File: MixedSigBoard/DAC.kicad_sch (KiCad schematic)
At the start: 17 parts

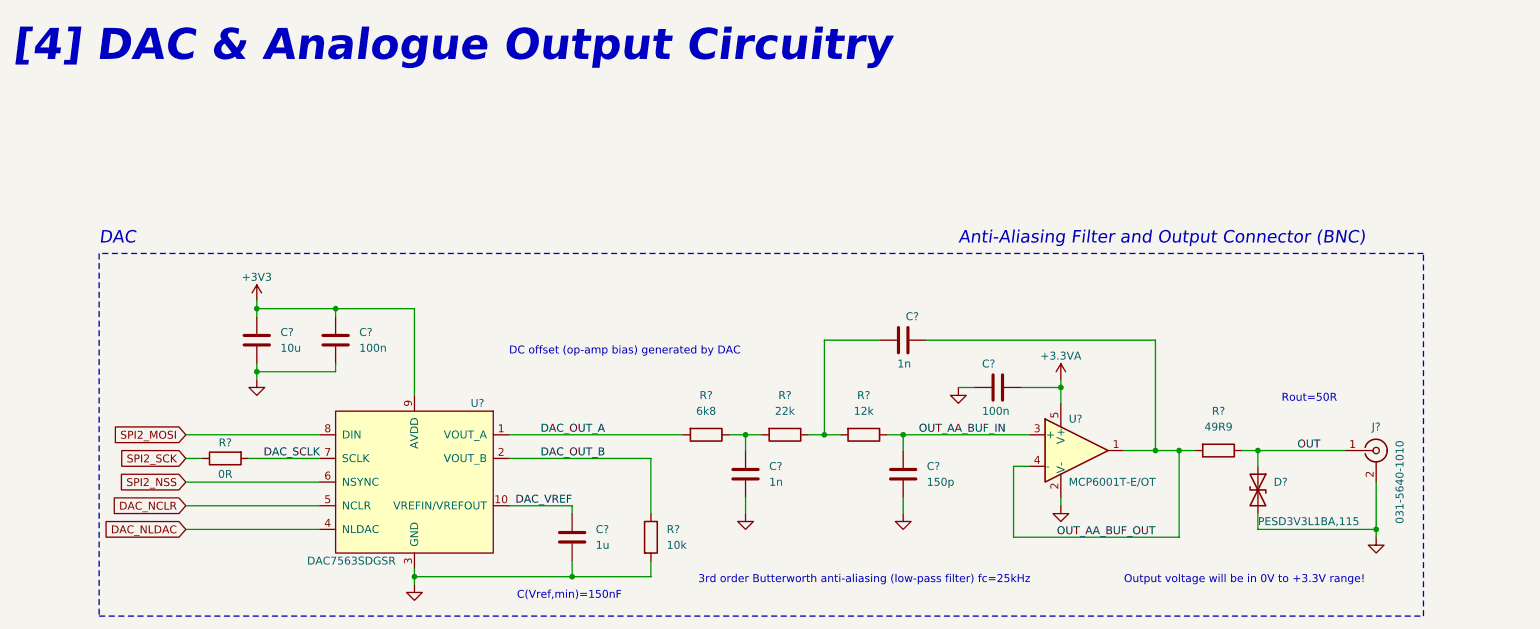
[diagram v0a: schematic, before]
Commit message: -Renumber components to match sheet number -Created PCB Constraints and Set-up
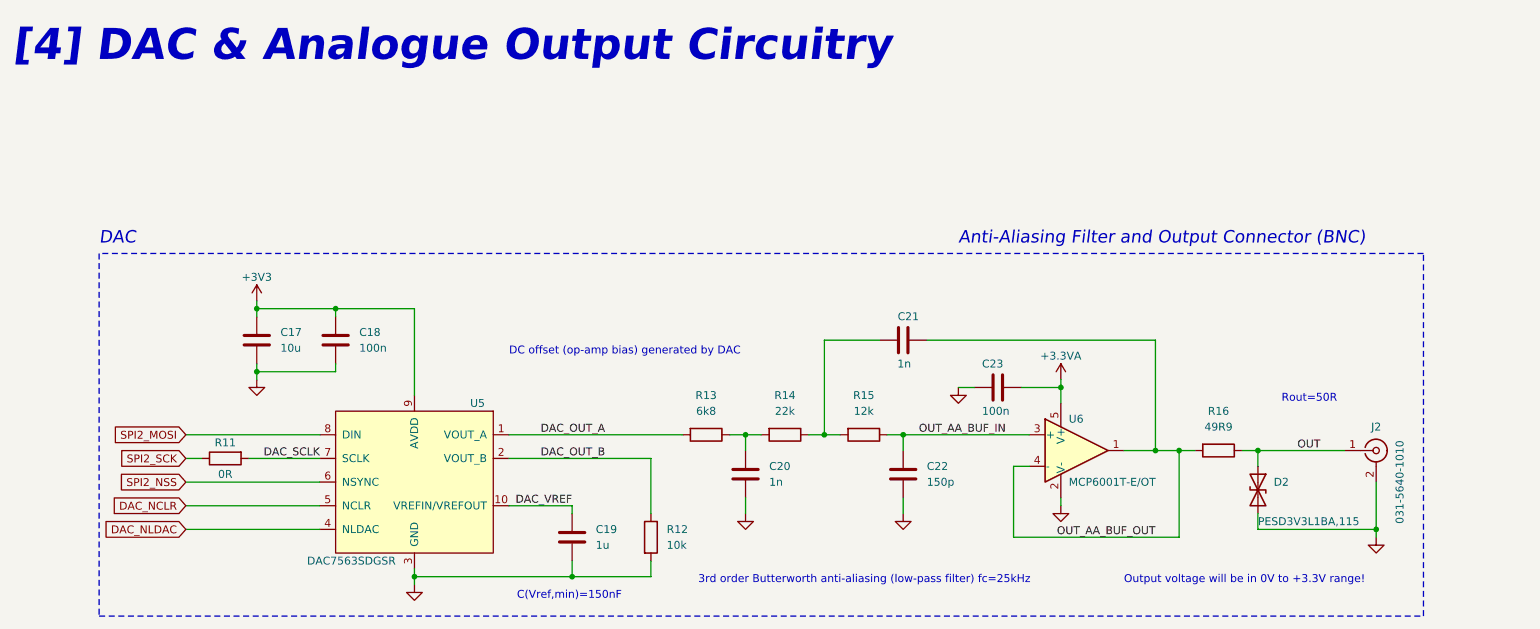
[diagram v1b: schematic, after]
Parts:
- gave numbers to parts that had none: 17

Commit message: Add all footprints
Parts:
- J2: footprint PhilsLab_Footprints_KiCad6:AMPHENOL-BNC-031-5640-1010 -> MixSig_Footprints_KiCad6:AMPHENOL-BNC-031-5640-1010
- U5: footprint PhilsLab_Footprints_KiCad6:VSSOP-10 -> MixSig_Footprints_KiCad6:VSSOP-10
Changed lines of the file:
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@@
 			)
 		)
-		(property "Footprint" "PhilsLab_Footprints_KiCad6:VSSOP-10"
+		(property "Footprint" "MixSig_Footprints_KiCad6:VSSOP-10"
 			(at 88.9 105.41 0)
 			(effects
@@
 			)
 		)
-		(property "Footprint" "PhilsLab_Footprints_KiCad6:AMPHENOL-BNC-031-5640-1010"
+		(property "Footprint" "MixSig_Footprints_KiCad6:AMPHENOL-BNC-031-5640-1010"
 			(at 243.84 95.25 0)
 			(effects

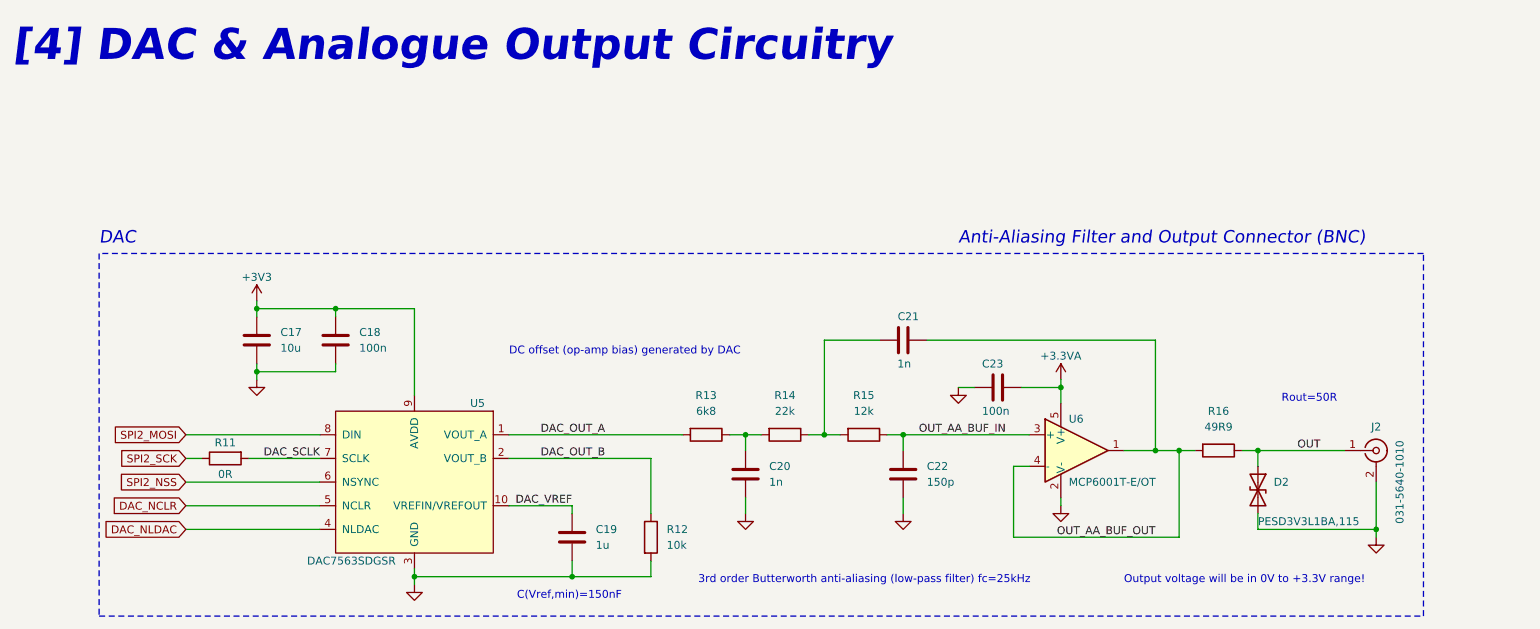
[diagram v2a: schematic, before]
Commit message: Layout w/o Traces for MCU, ADC page
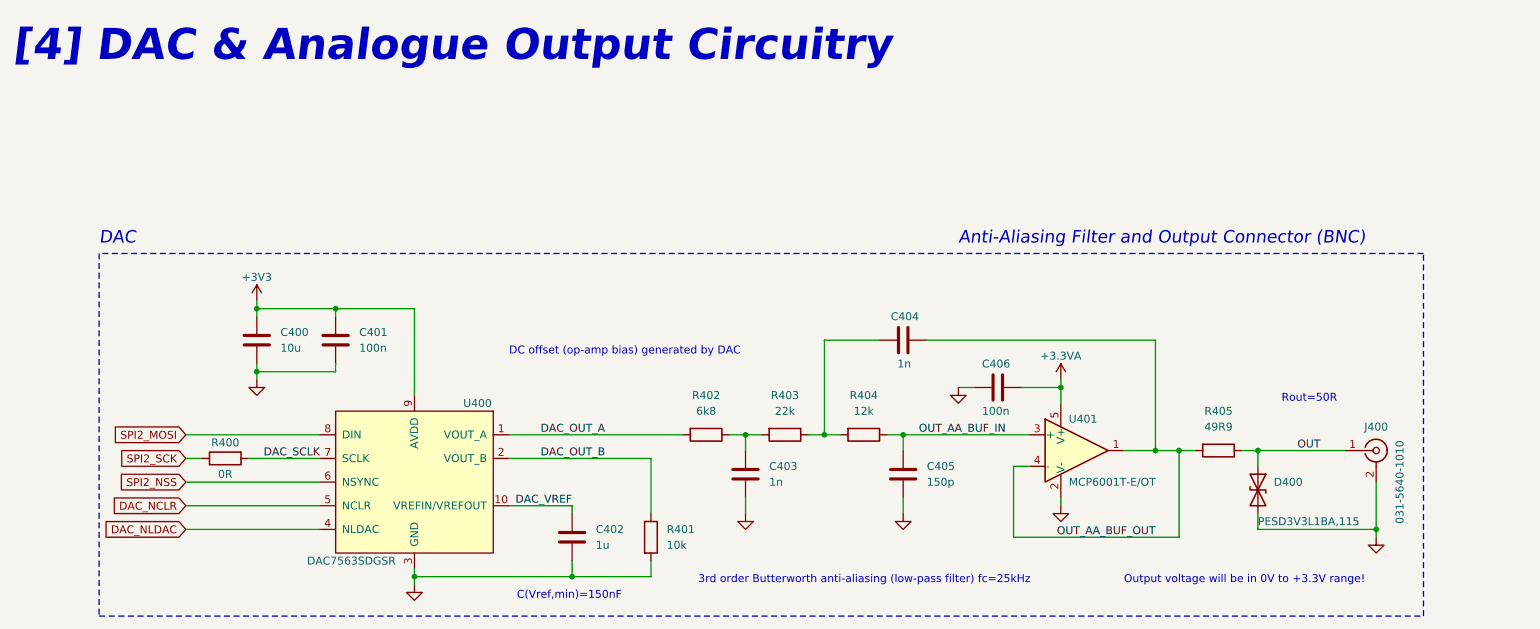
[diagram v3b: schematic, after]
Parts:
- renumbered C17 to C400, C18 to C401, C19 to C402, C20 to C403, C21 to C404, C22 to C405, C23 to C406, D2 to D400, J2 to J400, R11 to R400, R12 to R401, R13 to R402, R14 to R403, R15 to R404, R16 to R405, U5 to U400, U6 to U401
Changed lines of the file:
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@@
 		(on_board yes)
 		(dnp no)
-		(property "Reference" "R11"
+		(property "Reference" "R400"
 			(at 58.42 93.98 90)
 			(effects
@@
 			(project "MixSigPCB"
 				(path "/c49d23ab-146d-4089-864f-2d22b5b414b9/00000000-0000-0000-0000-000061c5ccf5"
-					(reference "R11")
+					(reference "R400")
 					(unit 1)
 				)
@@
 		(on_board yes)
 		(dnp no)
-		(property "Reference" "C19"
+		(property "Reference" "C402"
 			(at 118.11 107.95 0)
 			(effects
@@
 			(project "MixSigPCB"
 				(path "/c49d23ab-146d-4089-864f-2d22b5b414b9/00000000-0000-0000-0000-000061c5ccf5"
-					(reference "C19")
+					(reference "C402")
 					(unit 1)
 				)
@@
 		(on_board yes)
 		(dnp no)
-		(property "Reference" "C17"
+		(property "Reference" "C400"
 			(at 67.31 76.2 0)
 			(effects
@@
 			(project "MixSigPCB"
 				(path "/c49d23ab-146d-4089-864f-2d22b5b414b9/00000000-0000-0000-0000-000061c5ccf5"
-					(reference "C17")
+					(reference "C400")
 					(unit 1)
 				)
@@
 		(on_board yes)
 		(dnp no)
-		(property "Reference" "U5"
+		(property "Reference" "U400"
 			(at 99.06 87.63 0)
 			(effects
@@
 			(project "MixSigPCB"
 				(path "/c49d23ab-146d-4089-864f-2d22b5b414b9/00000000-0000-0000-0000-000061c5ccf5"
-					(reference "U5")
+					(reference "U400")
 					(unit 1)
 				)
@@
 		(on_board yes)
 		(dnp no)
-		(property "Reference" "C18"
+		(property "Reference" "C401"
 			(at 80.01 76.2 0)
 			(effects
@@
 			(project "MixSigPCB"
 				(path "/c49d23ab-146d-4089-864f-2d22b5b414b9/00000000-0000-0000-0000-000061c5ccf5"
-					(reference "C18")
+					(reference "C401")
 					(unit 1)
 				)
@@
 		(on_board yes)
 		(dnp no)
-		(property "Reference" "R12"
+		(property "Reference" "R401"
 			(at 129.54 107.95 0)
 			(effects
@@
 			(project "MixSigPCB"
 				(path "/c49d23ab-146d-4089-864f-2d22b5b414b9/00000000-0000-0000-0000-000061c5ccf5"
-					(reference "R12")
+					(reference "R401")
 					(unit 1)
 				)
@@
 		(on_board yes)
 		(dnp no)
-		(property "Reference" "U6"
+		(property "Reference" "U401"
 			(at 194.31 90.17 0)
 			(effects
@@
 			(project "MixSigPCB"
 				(path "/c49d23ab-146d-4089-864f-2d22b5b414b9/00000000-0000-0000-0000-000061c5ccf5"
-					(reference "U6")
+					(reference "U401")
 					(unit 1)
 				)
@@
 		(on_board yes)
 		(dnp no)
-		(property "Reference" "C23"
+		(property "Reference" "C406"
 			(at 180.34 81.28 90)
 			(effects
@@
 			(project "MixSigPCB"
 				(path "/c49d23ab-146d-4089-864f-2d22b5b414b9/00000000-0000-0000-0000-000061c5ccf5"
-					(reference "C23")
+					(reference "C406")
 					(unit 1)
 				)
@@
 		(on_board yes)
 		(dnp no)
-		(property "Reference" "R13"
+		(property "Reference" "R402"
 			(at 135.89 86.36 90)
 			(effects
@@
 			(project "MixSigPCB"
 				(path "/c49d23ab-146d-4089-864f-2d22b5b414b9/00000000-0000-0000-0000-000061c5ccf5"
-					(reference "R13")
+					(reference "R402")
 					(unit 1)
 				)
@@
 		(on_board yes)
 		(dnp no)
-		(property "Reference" "C20"
+		(property "Reference" "C403"
 			(at 146.05 97.79 0)
 			(effects
@@
 			(project "MixSigPCB"
 				(path "/c49d23ab-146d-4089-864f-2d22b5b414b9/00000000-0000-0000-0000-000061c5ccf5"
-					(reference "C20")
+					(reference "C403")
 					(unit 1)
 				)
@@
 		(on_board yes)
 		(dnp no)
-		(property "Reference" "R14"
+		(property "Reference" "R403"
 			(at 148.59 86.36 90)
 			(effects
@@
 			(project "MixSigPCB"
 				(path "/c49d23ab-146d-4089-864f-2d22b5b414b9/00000000-0000-0000-0000-000061c5ccf5"
-					(reference "R14")
+					(reference "R403")
 					(unit 1)
 				)
@@
 		(on_board yes)
 		(dnp no)
-		(property "Reference" "R15"
+		(property "Reference" "R404"
 			(at 161.29 86.36 90)
 			(effects
@@
 			(project "MixSigPCB"
 				(path "/c49d23ab-146d-4089-864f-2d22b5b414b9/00000000-0000-0000-0000-000061c5ccf5"
-					(reference "R15")
+					(reference "R404")
 					(unit 1)
 				)
@@
 		(on_board yes)
 		(dnp no)
-		(property "Reference" "C22"
+		(property "Reference" "C405"
 			(at 171.45 97.79 0)
 			(effects
@@
 			(project "MixSigPCB"
 				(path "/c49d23ab-146d-4089-864f-2d22b5b414b9/00000000-0000-0000-0000-000061c5ccf5"
-					(reference "C22")
+					(reference "C405")
 					(unit 1)
 				)
@@
 		(on_board yes)
 		(dnp no)
-		(property "Reference" "R16"
+		(property "Reference" "R405"
 			(at 218.44 88.9 90)
 			(effects
@@
 			(project "MixSigPCB"
 				(path "/c49d23ab-146d-4089-864f-2d22b5b414b9/00000000-0000-0000-0000-000061c5ccf5"
-					(reference "R16")
+					(reference "R405")
 					(unit 1)
 				)
@@
 		(on_board yes)
 		(dnp no)
-		(property "Reference" "D2"
+		(property "Reference" "D400"
 			(at 227.33 100.33 90)
 			(effects
@@
 			(project "MixSigPCB"
 				(path "/c49d23ab-146d-4089-864f-2d22b5b414b9/00000000-0000-0000-0000-000061c5ccf5"
-					(reference "D2")
+					(reference "D400")
 					(unit 1)
 				)
@@
 		(on_board yes)
 		(dnp no)
-		(property "Reference" "J2"
+		(property "Reference" "J400"
 			(at 243.84 91.44 0)
 			(effects
@@
 			(project "MixSigPCB"
 				(path "/c49d23ab-146d-4089-864f-2d22b5b414b9/00000000-0000-0000-0000-000061c5ccf5"
-					(reference "J2")
+					(reference "J400")
 					(unit 1)
 				)
@@
 		(on_board yes)
 		(dnp no)
-		(property "Reference" "C21"
+		(property "Reference" "C404"
 			(at 170.18 73.66 90)
 			(effects
@@
 			(project "MixSigPCB"
 				(path "/c49d23ab-146d-4089-864f-2d22b5b414b9/00000000-0000-0000-0000-000061c5ccf5"
-					(reference "C21")
-					(unit 1)
-				)
+					(reference "C404")
+					(unit 1)
+				)

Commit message: updated PCB footprints
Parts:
- J400: footprint MixSig_Footprints_KiCad6:AMPHENOL-BNC-031-5640-1010 -> MixSig_Footprints.pretty:AMPHENOL-BNC-031-5640-1010
- U400: footprint MixSig_Footprints_KiCad6:VSSOP-10 -> MixSig_Footprints.pretty:VSSOP-10
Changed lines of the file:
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@@
 			)
 		)
-		(property "Footprint" "MixSig_Footprints_KiCad6:VSSOP-10"
+		(property "Footprint" "MixSig_Footprints.pretty:VSSOP-10"
 			(at 88.9 105.41 0)
 			(effects
@@
 			)
 		)
-		(property "Footprint" "MixSig_Footprints_KiCad6:AMPHENOL-BNC-031-5640-1010"
+		(property "Footprint" "MixSig_Footprints.pretty:AMPHENOL-BNC-031-5640-1010"
 			(at 243.84 95.25 0)
 			(effects

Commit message: complete the MixSigPCB
-Created Gerber file and compressed to .zip
-created placement file
-filled all components from Mouser/JLCPCB/Digikey
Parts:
- C400: Manufacturer (none) -> TAIYO YUDEN; Manufacturer Part Number (none) -> MLASL168BB5106MTNB33
- C401, C406: Manufacturer (none) -> TAIYO YUDEN; Manufacturer Part Number (none) -> LMK105B7104KVHF
- C402: Manufacturer (none) -> YAGEO; Manufacturer Part Number (none) -> CC0603KRX5R6BB105
- C403, C404: Manufacturer (none) -> KYOCERA AVX; Manufacturer Part Number (none) -> 04025C102KAZ2A
- C405: Manufacturer (none) -> KEMET; Manufacturer Part Number (none) -> C0402C151J1GACAUTO
- D400: Manufacturer (none) -> NEXPERIA USA INC.; Manufacturer Part Number (none) -> PESD3V3L1BA,115
- J400: Manufacturer (none) -> AMPHENOL RF; Manufacturer Part Number (none) -> 31-5640-1010
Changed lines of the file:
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@@
 			)
 		)
-		(property "Datasheet" "~"
+		(property "Datasheet" "https://www.mouser.com/datasheet/3/508/1/upy-gphc_x5r_4v-to-50v.pdf"
 			(at 114.3 109.22 0)
 			(effects
@@
 					(size 1.27 1.27)
 				)
+			)
+		)
+		(property "Manufacturer" "YAGEO"
+			(at 114.3 109.22 0)
+			(effects
+				(font
+					(size 1.27 1.27)
+				)
+				(hide yes)
+			)
+		)
+		(property "Manufacturer Part Number" "CC0603KRX5R6BB105"
+			(at 114.3 109.22 0)
+			(effects
+				(font
+					(size 1.27 1.27)
+				)
+				(hide yes)
 			)
 		)
@@
 			)
 		)
-		(property "Datasheet" "~"
+		(property "Datasheet" "https://ds.yuden.co.jp/TYCOMPAS/or/download?pn=MLAST063SCG681JFNA01&fileType=CA"
 			(at 63.5 77.47 0)
 			(effects
@@
 					(size 1.27 1.27)
 				)
+			)
+		)
+		(property "Manufacturer" "TAIYO YUDEN"
+			(at 63.5 77.47 0)
+			(effects
+				(font
+					(size 1.27 1.27)
+				)
+				(hide yes)
+			)
+		)
+		(property "Manufacturer Part Number" "MLASL168BB5106MTNB33"
+			(at 63.5 77.47 0)
+			(effects
+				(font
+					(size 1.27 1.27)
+				)
+				(hide yes)
 			)
 		)
@@
 			)
 		)
-		(property "Datasheet" "~"
+		(property "Datasheet" "https://www.mouser.com/catalog/specsheets/taiyo%20yuden_12132018_mlcc11_hq_e.pdf"
 			(at 76.2 77.47 0)
 			(effects
@@
 					(size 1.27 1.27)
 				)
+			)
+		)
+		(property "Manufacturer" "TAIYO YUDEN"
+			(at 76.2 77.47 0)
+			(effects
+				(font
+					(size 1.27 1.27)
+				)
+				(hide yes)
+			)
+		)
+		(property "Manufacturer Part Number" "LMK105B7104KVHF"
+			(at 76.2 77.47 0)
+			(effects
+				(font
+					(size 1.27 1.27)
+				)
+				(hide yes)
 			)
 		)
@@
 			)
 		)
-		(property "Datasheet" "~"
+		(property "Datasheet" "https://www.mouser.com/catalog/specsheets/taiyo%20yuden_12132018_mlcc11_hq_e.pdf"
 			(at 182.88 85.09 0)
 			(effects
@@
 					(size 1.27 1.27)
 				)
+			)
+		)
+		(property "Manufacturer" "TAIYO YUDEN"
+			(at 182.88 85.09 90)
+			(effects
+				(font
+					(size 1.27 1.27)
+				)
+				(hide yes)
+			)
+		)
+		(property "Manufacturer Part Number" "LMK105B7104KVHF"
+			(at 182.88 85.09 90)
+			(effects
+				(font
+					(size 1.27 1.27)
+				)
+				(hide yes)
 			)
 		)
@@
 			)
 		)
-		(property "Datasheet" "~"
+		(property "Datasheet" "https://datasheets.kyocera-avx.com/X7RDielectric.pdf"
 			(at 142.24 99.06 0)
 			(effects
@@
 					(size 1.27 1.27)
 				)
+			)
+		)
+		(property "Manufacturer" "KYOCERA AVX"
+			(at 142.24 99.06 0)
+			(effects
+				(font
+					(size 1.27 1.27)
+				)
+				(hide yes)
+			)
+		)
+		(property "Manufacturer Part Number" "04025C102KAZ2A"
+			(at 142.24 99.06 0)
+			(effects
+				(font
+					(size 1.27 1.27)
+				)
+				(hide yes)
 			)
 		)
@@
 			)
 		)
-		(property "Datasheet" "~"
+		(property "Datasheet" "https://www.mouser.com/datasheet/3/72/1/KEM_C1022_C0G_AUTO_SMD.pdf"
 			(at 167.64 99.06 0)
 			(effects
@@
 					(size 1.27 1.27)
 				)
+			)
+		)
+		(property "Manufacturer" "KEMET"
+			(at 167.64 99.06 0)
+			(effects
+				(font
+					(size 1.27 1.27)
+				)
+				(hide yes)
+			)
+		)
+		(property "Manufacturer Part Number" "C0402C151J1GACAUTO"
+			(at 167.64 99.06 0)
+			(effects
+				(font
+					(size 1.27 1.27)
+				)
+				(hide yes)
 			)
 		)
@@
 			)
 		)
-		(property "Datasheet" "~"
+		(property "Datasheet" "https://assets.nexperia.com/documents/data-sheet/PESD3V3L1BA.pdf"
 			(at 224.79 101.6 0)
 			(effects
@@
 			)
 		)
+		(property "Manufacturer" "NEXPERIA USA INC."
+			(at 224.79 101.6 90)
+			(effects
+				(font
+					(size 1.27 1.27)
+				)
+				(hide yes)
+			)
+		)
+		(property "Manufacturer Part Number" "  PESD3V3L1BA,115"
+			(at 224.79 101.6 90)
+			(effects
+				(font
+					(size 1.27 1.27)
+				)
+				(hide yes)
+			)
+		)
 		(pin "1"
 		)
@@
 			)
 		)
-		(property "Datasheet" " ~"
+		(property "Datasheet" "https://mm.digikey.com/Volume0/opasdata/d220001/medias/docus/6155/tmp_187197.tmp.pdf?_gl=1*1n1llfl*_up*MQ..*_gs*MQ..&gclid=CjwKCAiA9aPKBhBhEiwAyz82J4f1O4zMCAdvZNCPIwXwXPQZRdXxNWOUcwHTwizcCYFCZ3Nzs2sUtRoCiX8QAvD_BwE&gclsrc=aw.ds&gbraid=0AAAAADrbLlhXEbj6OgaL832YKP-dk4gv7"
 			(at 243.84 95.25 0)
 			(effects
@@
 			)
 		)
+		(property "Manufacturer" "AMPHENOL RF"
+			(at 243.84 95.25 0)
+			(effects
+				(font
+					(size 1.27 1.27)
+				)
+				(hide yes)
+			)
+		)
+		(property "Manufacturer Part Number" "31-5640-1010"
+			(at 243.84 95.25 0)
+			(effects
+				(font
+					(size 1.27 1.27)
+				)
+				(hide yes)
+			)
+		)
 		(pin "1"
 		)
@@
 			)
 		)
-		(property "Datasheet" "~"
+		(property "Datasheet" "https://datasheets.kyocera-avx.com/X7RDielectric.pdf"
 			(at 167.64 77.47 0)
 			(effects
@@
 			)
 		)
+		(property "Manufacturer" "KYOCERA AVX"
+			(at 167.64 77.47 90)
+			(effects
+				(font
+					(size 1.27 1.27)
+				)
+				(hide yes)
+			)
+		)
+		(property "Manufacturer Part Number" "04025C102KAZ2A"
+			(at 167.64 77.47 90)
+			(effects
+				(font
+					(size 1.27 1.27)
+				)
+				(hide yes)
+			)
+		)
